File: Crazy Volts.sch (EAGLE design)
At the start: 3 parts, among them U1 ATMEGA328P-PU

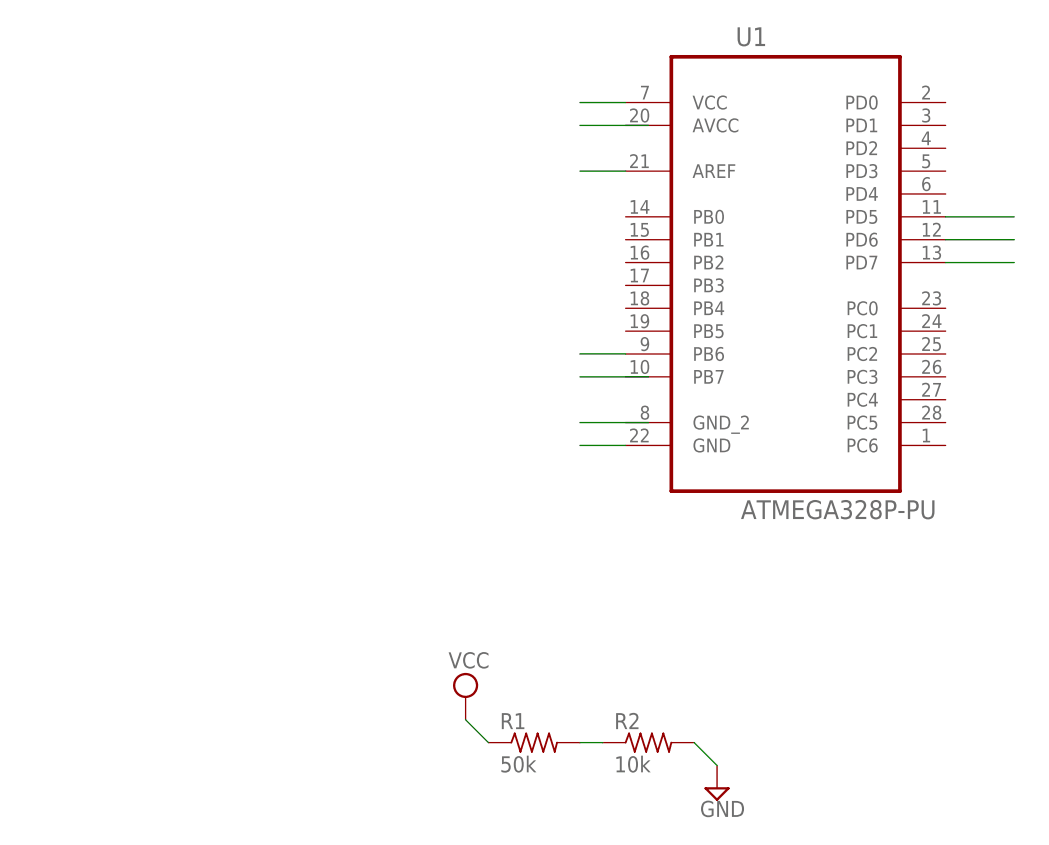
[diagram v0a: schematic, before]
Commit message: final board; initial timekeeper
using a teensy + batt + xtal for timekeeping
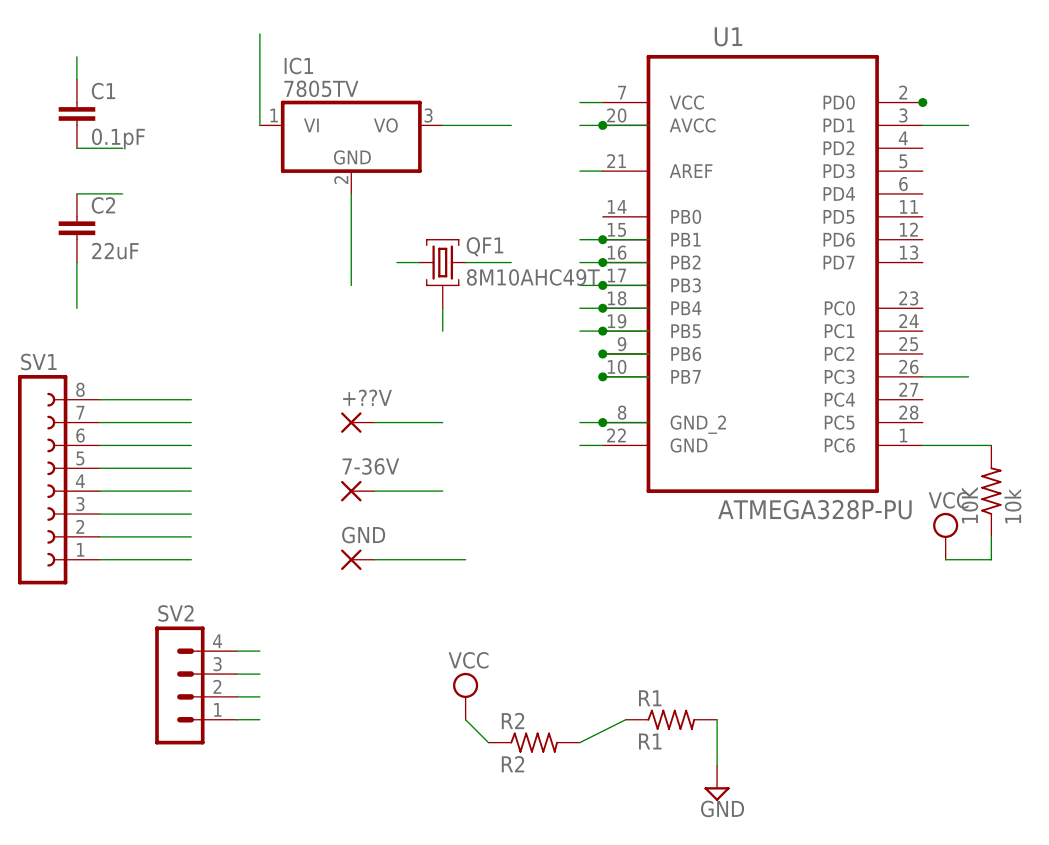
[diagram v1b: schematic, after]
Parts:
- added +??V, 7-36V, GND: (no value), wirepad:1,6/0,9
- added 10K: 10k, rcl:R-US_0207/7
- added C1: 0.1pF, capacitor-wima:C5/2.5
- added C2: 22uF, capacitor-wima:C2.5/5
- added IC1: 7805TV, linear:7805TV
- added QF1: 8M10AHC49T, crystal:8M10AHC49T
- added SV1: (no value), con-lsta:FE08-1
- added SV2: (no value), con-lstb:MA04-1
- R1: value 50k -> R1
- R2: value 10k -> R2
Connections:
- new net 3V3: SV1.6
- new net DISP_CLK: SV1.2, U1.PB2
- new net IC10: QF1.1, U1.PB7
- new net IC9: QF1.3, U1.PB6
- new net RST: 10K.2, SV2.4, U1.PC6
- new net RX: SV2.3, U1.PD0
- new net TX: SV2.2, U1.PD1
- new net VIN: 7-36V.P, C2.1, IC1.VI
- net DISP_CS: now also SV1.5, U1.PB4; no longer U1.PD6
- net DISP_DATA: now also SV1.1, U1.PB1; no longer U1.PB6
- net DISP_DC: now also SV1.3, U1.PB3; no longer U1.PD5
- net DISP_RST: now also SV1.4, U1.PB5; no longer U1.PD7
- net GND: now also C1.2, C2.2, GND.P, IC1.GND, QF1.2, R1.2, SV1.8, SV2.1, U1.GND_2; no longer R2.2
- net VBATT: now also +??V.P, R2.1; no longer R1.1
- net VCC: now also 10K.1, C1.1, IC1.VO, SV1.7, U1.AVCC
- net VSENSE: now also R1.1, R2.2, U1.PC3; no longer R1.2, R2.1
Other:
- moved on the sheet: R1, R2, U1
